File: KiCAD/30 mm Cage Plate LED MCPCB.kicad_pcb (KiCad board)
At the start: 2 copper layers, 40 x 40 mm, 15 parts, among them IC1 AL8843QSP-13, J1 Conn_01x04

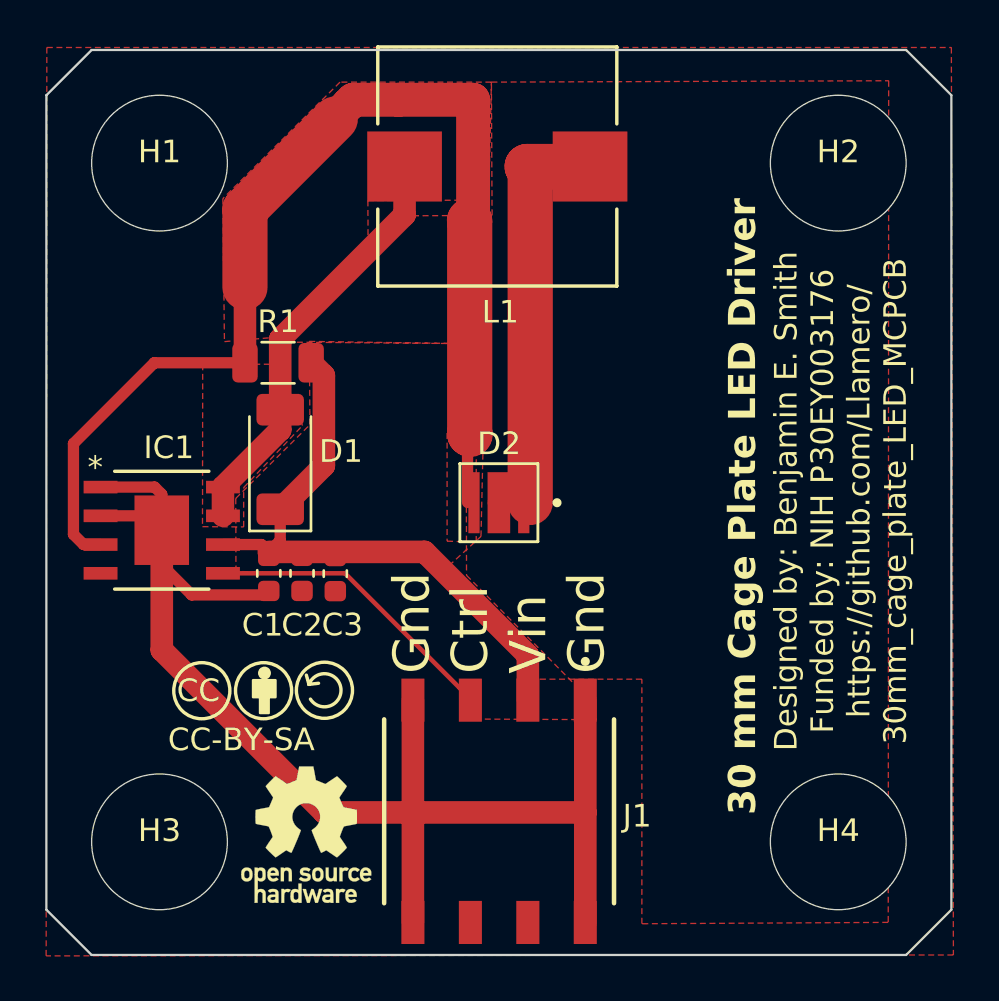
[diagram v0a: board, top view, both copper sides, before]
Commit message: Move PWM and Vin pins apart to prevent fatal shorts of Vin to Ctrl
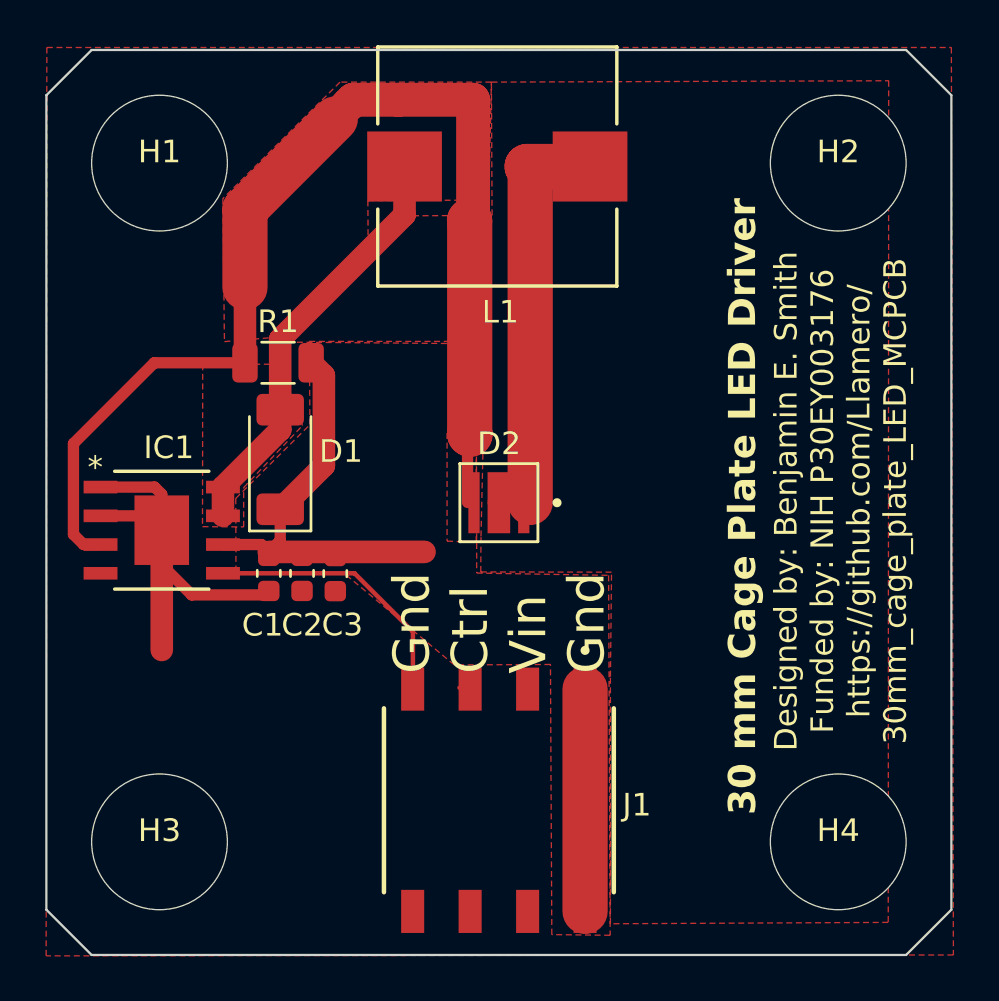
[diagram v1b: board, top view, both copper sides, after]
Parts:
- removed REF**: CC-BY-SA Symbol, Custom:CC-BY-SA Symbol
- removed REF**: OSHW-Logo_5.7x6mm_SilkScreen, Symbol:OSHW-Logo_5.7x6mm_SilkScreen
- moved J1 0.49 mm to (120.0, 93.2)
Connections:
- J1 pad 1: GND -> /Vin
- J1 pad 2: /Vin -> GND
- J1 pad 3: /PWM -> GND
- J1 pad 4: GND -> /PWM
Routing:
- net GND: track 60.8 -> 20.5 mm
- net /Vin: track 27.1 -> 28.5 mm
- net /PWM: track 13.5 -> 12.5 mm

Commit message: working draft
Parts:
- removed D2: SST-10-IRD-B90H-S810, Custom:LED_SST-10-IRD-B90H-S810
- added D3: LED_Pad, Custom:LED_XLAMP_XE-G_CRW, F.Cu at (119.2, 78.9)
- added D4: LED_Pad, Custom:LED_XLAMP_XE-G_CRW, F.Cu at (120.8, 78.9)
- added D5: LED_Pad, Custom:LED_XLAMP_XE-G_CRW, F.Cu at (120.8, 81.1)
- added D6: LED_Pad, Custom:LED_XLAMP_XE-G_CRW, F.Cu at (119.2, 81.1)
- added RN1: 180, Resistor_SMD:R_Array_Convex_8x0602, F.Cu at (125.3, 85.6)
- added U2: TLP3480, Custom:TLP3480-SSR, F.Cu at (128.8, 67.7)
- added U3: TLP3480, Custom:TLP3480-SSR, F.Cu at (128.8, 71.6)
- added U4: TLP3480, Custom:TLP3480-SSR, F.Cu at (128.8, 75.5)
- added U5: TLP3480, Custom:TLP3480-SSR, F.Cu at (128.8, 79.5)
- C1, C2, C3: value 10μF -> 22μF; footprint Capacitor_SMD:C_0603_1608Metric -> Capacitor_SMD:C_0805_2012Metric
- J1: value Conn_01x04 -> Conn_01x08_Socket; footprint Custom:SAMTEC_SSM-104-L-SH -> Custom:SAMTEC_SSM-108-F-SH-TR
- R1: value 0.068 -> 0.040
- moved C3 1.02 mm to (113.8, 83.1)
- moved J1 0.73 mm to (120.0, 93.9), turned to 0 degrees
- moved C2 0.51 mm to (111.8, 83.1)
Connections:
- net Net-(IC1-SET) renamed /LED+
- J1 pad 1: /Vin -> /PWM
- J1 pad 3: GND -> /Vin
- J1 pad 4: /PWM -> GND
- L1 pad 1: Net-(D2-PadC) -> /LED-
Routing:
- net GND: track 20.5 -> 48.3 mm
- net Net-(RN1-R1.1): track 0.00 -> 23.7 mm
- net Net-(D2-PadC): track 21.7 -> 0.00 mm
- net Net-(RN1-R2.1): track 0.00 -> 21.3 mm
- net Net-(RN1-R3.1): track 0.00 -> 19.6 mm
- net Net-(RN1-R4.1): track 0.00 -> 17.2 mm
- net Net-(RN1-R5.1): track 0.00 -> 15.6 mm
- net /LED-: track 0.00 -> 13.8 mm
- net Net-(D3-K): track 0.00 -> 13.8 mm
- net Net-(RN1-R6.1): track 0.00 -> 13.1 mm
- net Net-(RN1-R7.1): track 0.00 -> 11.4 mm
- net Net-(D6-K): track 0.00 -> 11.4 mm
- net Net-(D5-K): track 0.00 -> 11.0 mm
- net /Vin: track 28.5 -> 18.7 mm
- net Net-(D4-K): track 0.00 -> 9.27 mm
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- added copper zone on F.Cu, net /LED-
- removed copper zone on F.Cu, net Net-(D2-PadC)
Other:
- board text removed: "Gnd Ctrl Vin Gnd"

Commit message: Before adding mux to PCB
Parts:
- added R2: 0, Resistor_SMD:R_1206_3216Metric, F.Cu at (125.9, 72.9)
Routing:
- net Net-(D4-K): track 9.27 -> 10.3 mm
- net Net-(D5-K): track 11.0 -> 12.1 mm

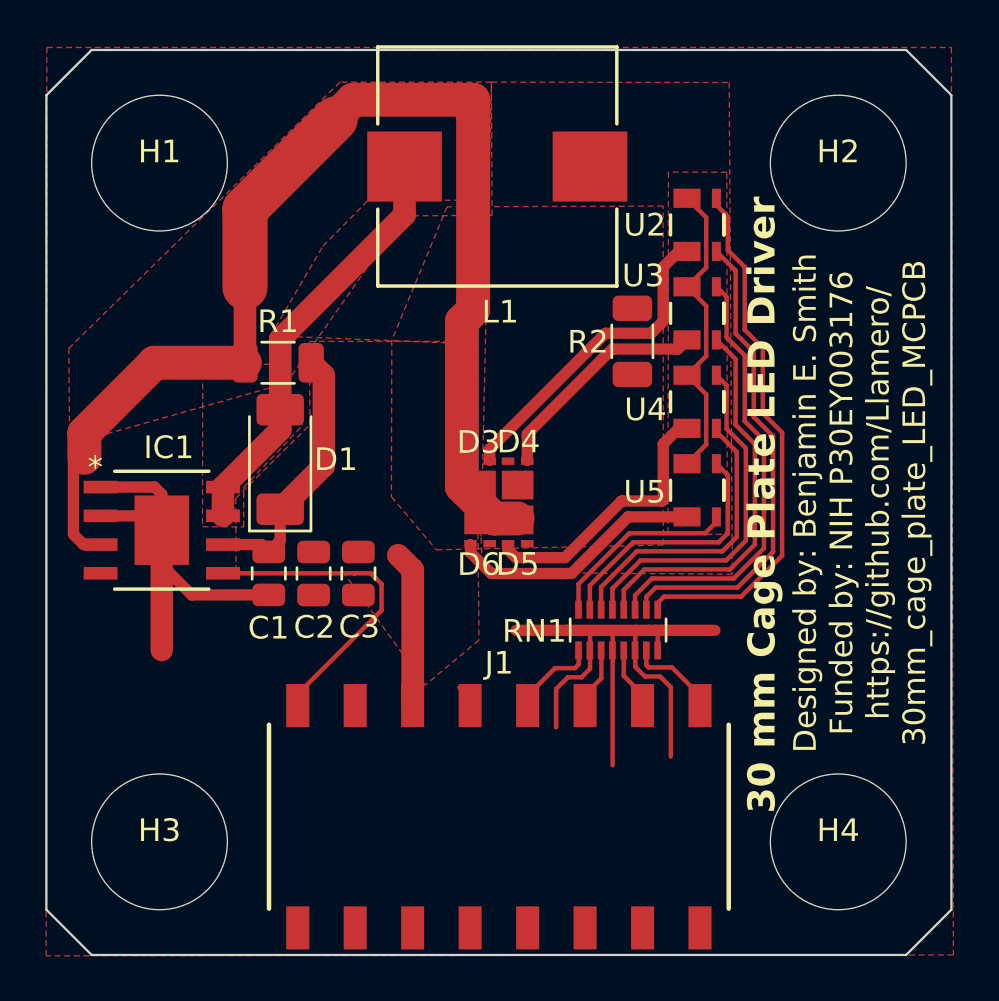
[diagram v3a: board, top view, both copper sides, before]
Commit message: Fan added
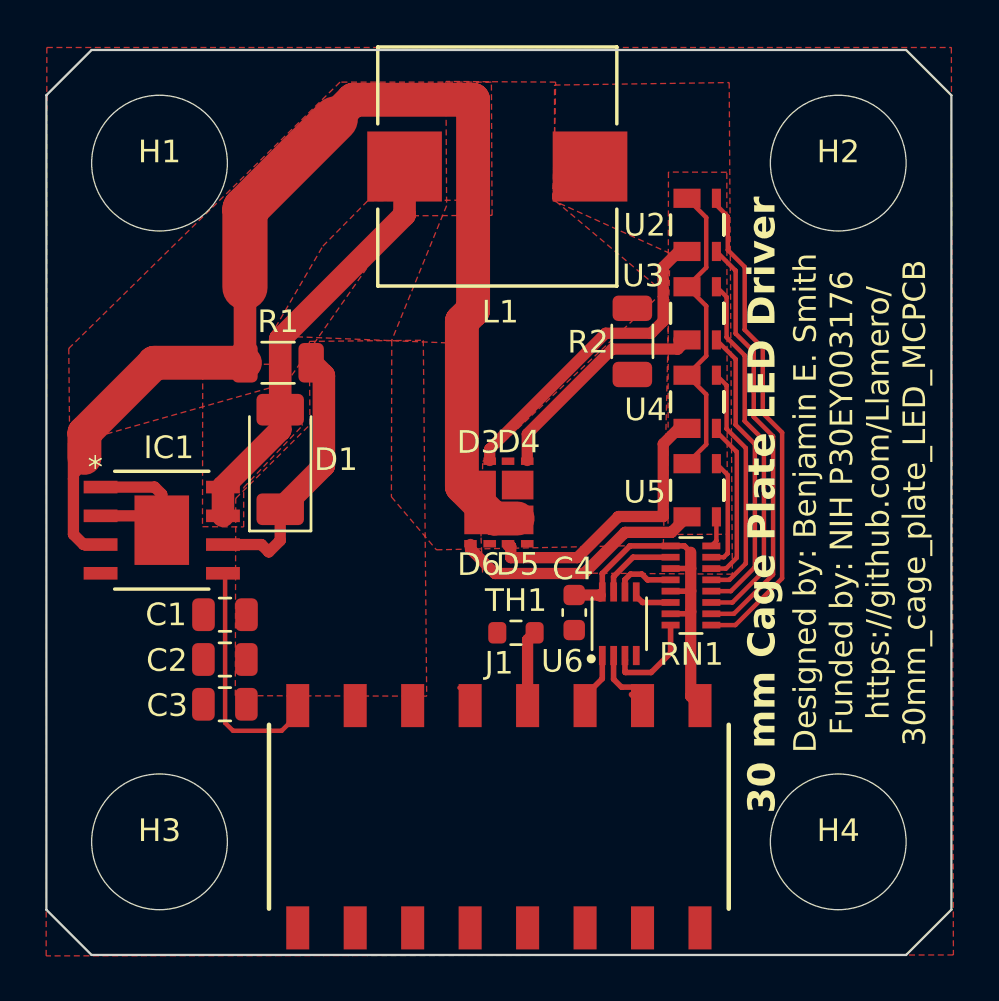
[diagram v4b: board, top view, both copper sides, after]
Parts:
- added C4: 0.1μF, Capacitor_SMD:C_0603_1608Metric, F.Cu at (123.3, 84.9)
- added TH1: Thermistor, Resistor_SMD:R_0603_1608Metric, F.Cu at (120.8, 85.8)
- added U6: SN74LVC1G139DCUR, Custom:SOP50P310X90-8N, F.Cu at (125.3, 85.4)
- moved C3 8.26 mm to (107.9, 88.9), turned to 0 degrees
- moved C2 5.46 mm to (107.9, 86.9), turned to 0 degrees
- moved RN1 3.77 mm to (128.5, 83.7), turned to 180 degrees
- moved C1 2.66 mm to (107.9, 85.0), turned to 0 degrees
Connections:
- J1 pad 5: /D -> /Temp
- J1 pad 6: /C -> /A
- J1 pad 8: /A -> /5V
- RN1 pad 10: GND -> /1
- RN1 pad 11: /C -> /5V
- RN1 pad 12: GND -> /2
- RN1 pad 13: /B -> /5V
- RN1 pad 14: GND -> /3
- RN1 pad 15: /A -> /5V
- RN1 pad 16: GND -> /4
- RN1 pad 9: /D -> /5V
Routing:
- net GND: track 48.1 -> 8.38 mm
- net /5V: track 0.00 -> 16.4 mm
- net Net-(RN1-R8.1): track 8.59 -> 1.38 mm
- net /Vin: track 18.7 -> 11.8 mm
- net Net-(RN1-R7.1): track 11.4 -> 4.96 mm
- net Net-(RN1-R6.1): track 13.1 -> 7.41 mm
- net Net-(RN1-R5.1): track 15.6 -> 10.7 mm
- net /4: track 0.00 -> 4.38 mm
- net Net-(RN1-R4.1): track 17.2 -> 13.1 mm
- net /D: track 3.88 -> 0.00 mm
- net /1: track 0.00 -> 3.74 mm
- net /Temp: track 0.00 -> 3.35 mm
- net Net-(RN1-R3.1): track 19.6 -> 16.3 mm
- net /2: track 0.00 -> 2.95 mm
- net /PWM: track 14.1 -> 11.2 mm
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
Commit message: Add logo
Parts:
- added REF**: CC-BY-SA Symbol, Custom:CC-BY-SA Symbol, F.Cu at (114.6, 84.5)
- moved C4 0.34 mm to (123.6, 85.0)
- moved U6 0.31 mm to (125.6, 85.3)
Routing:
- net /B: track 2.68 -> 3.32 mm

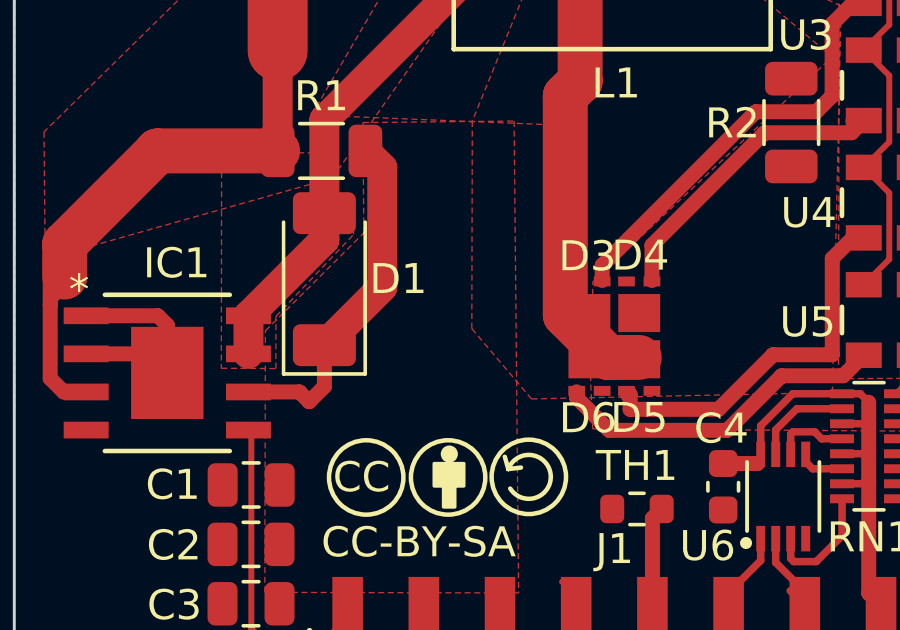
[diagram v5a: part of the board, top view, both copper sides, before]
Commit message: Add OSHW logo
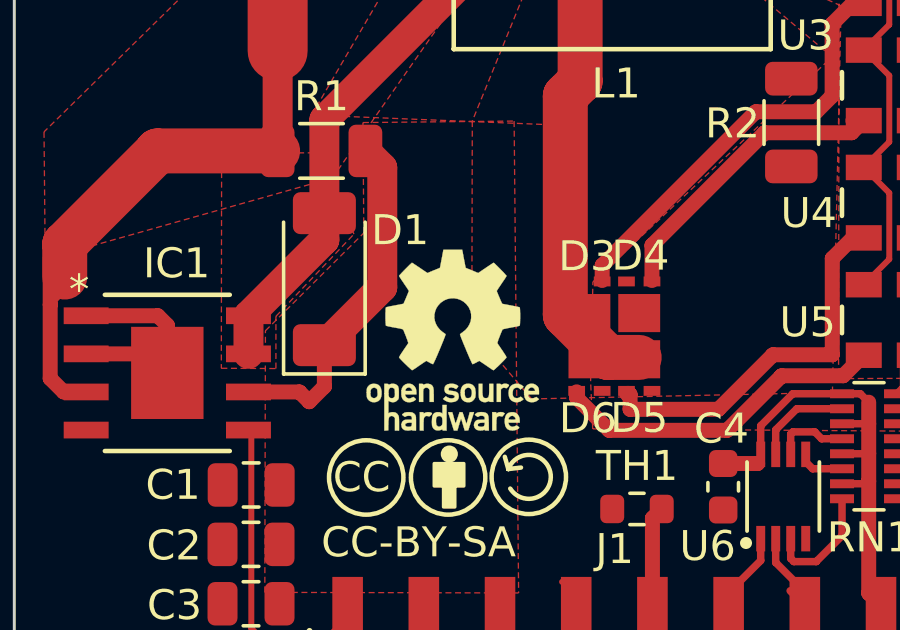
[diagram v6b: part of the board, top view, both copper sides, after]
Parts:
- added REF**: OSHW-Logo_5.7x6mm_SilkScreen, Symbol:OSHW-Logo_5.7x6mm_SilkScreen, F.Cu at (114.6, 80.1)

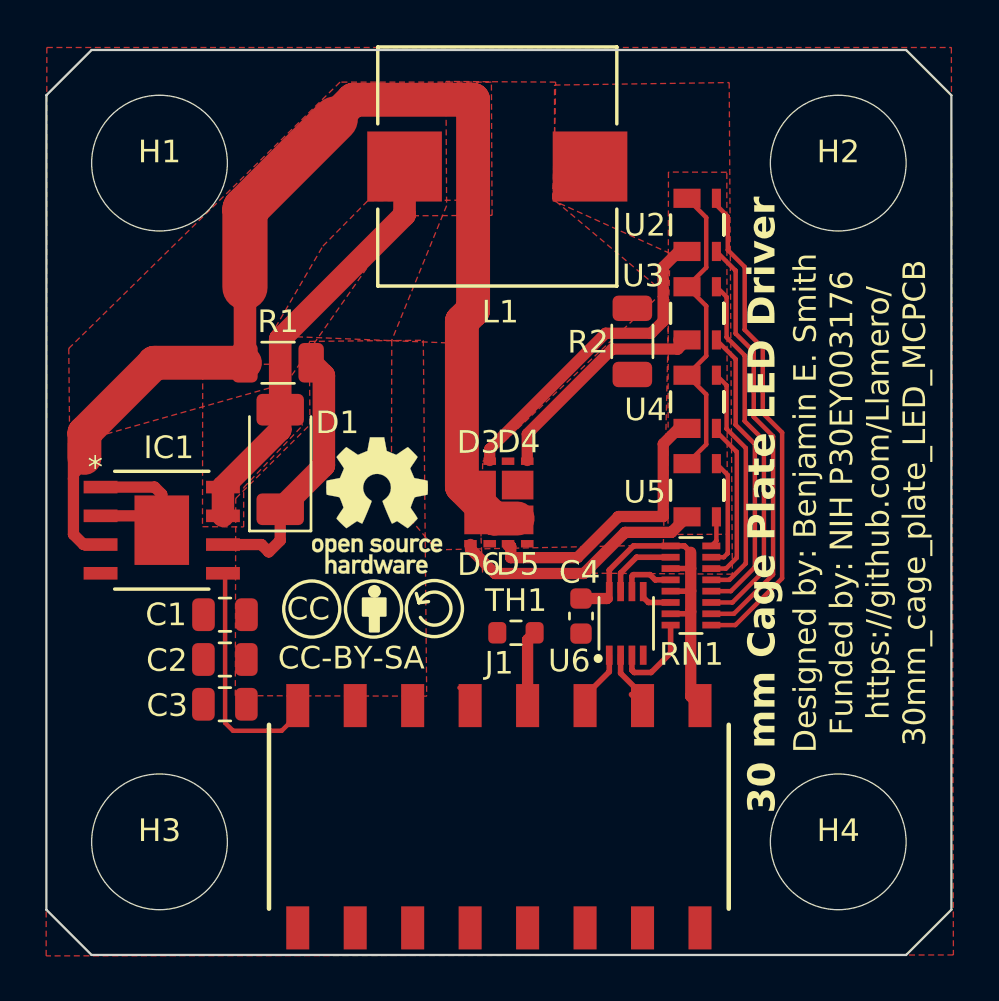
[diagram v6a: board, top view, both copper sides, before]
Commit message: More copper for LEDs, OSHW logo
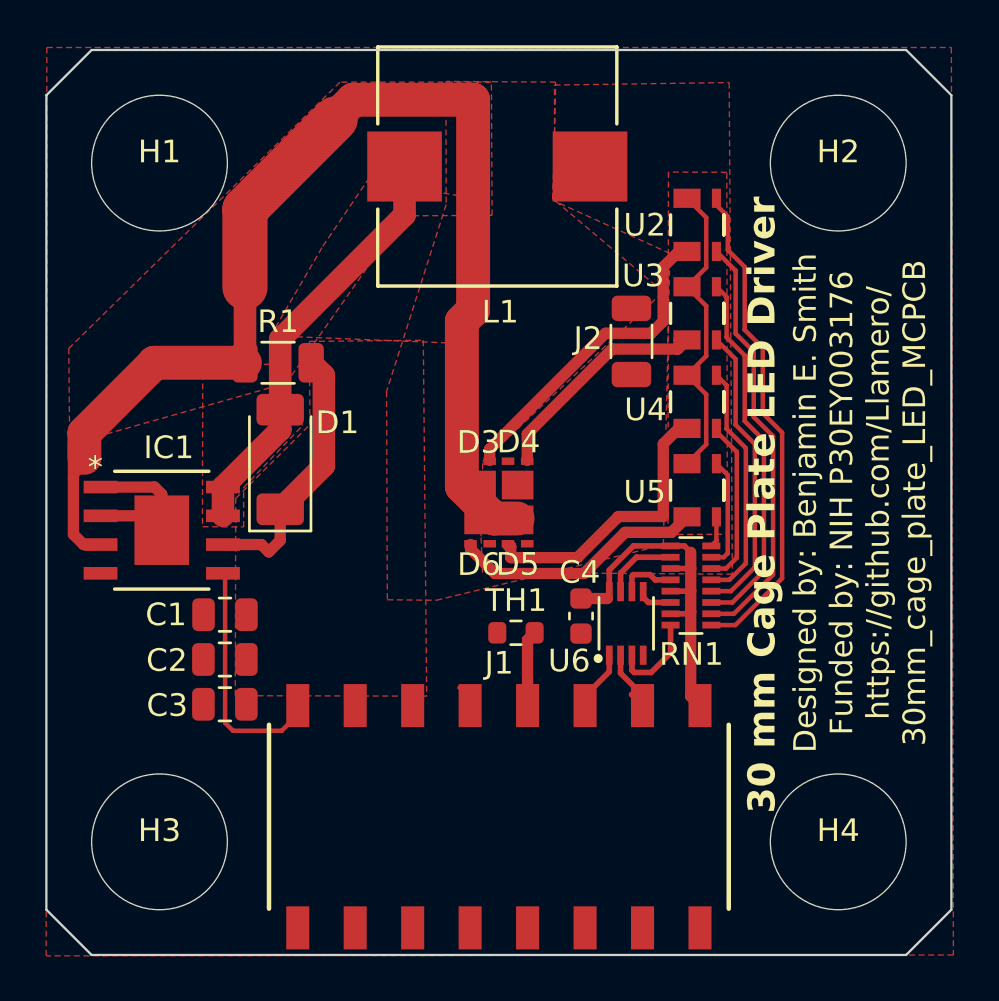
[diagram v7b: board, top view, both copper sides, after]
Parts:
- removed R2: 0, Resistor_SMD:R_1206_3216Metric
- removed REF**: OSHW-Logo_5.7x6mm_SilkScreen, Symbol:OSHW-Logo_5.7x6mm_SilkScreen
- removed REF**: CC-BY-SA Symbol, Custom:CC-BY-SA Symbol
- added J2: 0, Resistor_SMD:R_1206_3216Metric, F.Cu at (125.9, 72.9)

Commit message: update
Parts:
- added SYM1: Logo_Open_Hardware_Small, Symbol:OSHW-Logo_5.7x6mm_SilkScreen, F.Cu at (114.6, 80.4)
- added SYM2: Logo_Open_Hardware_Small, Custom:CC-BY-SA Symbol, F.Cu at (114.6, 84.7)
